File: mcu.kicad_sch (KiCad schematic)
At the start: 20 parts, among them J12 MCU_GPIOS1, J4 MCU_GPIOS2, J5 FTDI_6P, J6 AVR-ISP-6, U2 ATmega168A-A, Y1 16M

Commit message: printed pdf from schematics
Signed-off-by: Mika Laitio <lamikr@gmail.com>
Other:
- company: (none) -> Mika Laitio
- title: (none) -> I2S Audio to AES/EBU Optical Toslink
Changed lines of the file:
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@@
   (paper "A4")
   (title_block
+    (title "I2S Audio to AES/EBU Optical Toslink")
     (date "2023-12-26")
     (rev "v0.1")
+    (company "Mika Laitio")
   )
   (junction (at 59.055 38.1) (diameter 0) (color 0 0 0 0)

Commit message: added mpn and sku_digikey numbers for bom
Signed-off-by: Mika Laitio <lamikr@gmail.com>
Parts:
- C10, C11: MFR (none) -> Murata; MPN (none) -> GJM1555C1H160GB01D; SKU_DIGIKEY (none) -> 490-8081-1-ND
- C12, C6, C7, C8, C9: MFR (none) -> Murata; MPN (none) -> GRM033R61A104ME15D; SKU_DIGIKEY (none) -> 490-5405-1-ND
- J4: MFR (none) -> Würth Elektronik; MPN (none) -> 61300311121; Price (none) -> 0.13; SKU_DIGIKEY (none) -> 732-5316-ND
- J5: Notes (none) -> 1x20; Price (none) -> 0.43; SKU_DIGIKEY (none) -> 10129378-920001BLF-ND
- J6: MFR (none) -> Amphenol ICC (FCI); MPN (none) -> 75869-131LF; Notes (none) -> 2x3 with plastic; Price (none) -> 0.88; SKU_DIGIKEY (none) -> 609-2845-ND
- R1, R3: MFR (none) -> Yageo; MPN (none) -> RC0402FR-074K7L; Price (none) -> 0.1; SKU_DIGIKEY (none) -> 311-4.7KLRCT-ND
- R2: MFR (none) -> Yageo; MPN (none) -> RC0402FR-071K5L; Price (none) -> 0.1; SKU_DIGIKEY (none) -> 311-1.50KLRCT-ND
- R4: MFR (none) -> Yageo; MPN (none) -> RC0402FR-070RL; Price (none) -> 0.1; SKU_DIGIKEY (none) -> 311-0.0LRCT-ND
- R5: MFR (none) -> Yageo; MPN (none) -> RC0402FR-0710KL; Price (none) -> 0.1; SKU_DIGIKEY (none) -> 311-10.0KLRCT-ND
- U2: MFR (none) -> Microshell; MPN (none) -> ATMEGA168A-AUR; Price (none) -> 2.36; SKU_DIGIKEY (none) -> ATMEGA168A-AURTR-ND
- Y1: MFR (none) -> Abracon LLC; MPN (none) -> ABM7-16.000MHZ-D2Y-T; Price (none) -> 0.67; SKU_DIGIKEY (none) -> 535-9840-1-ND; SKU_digikey 535-9840-1-ND -> (none)

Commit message: added led that was missing from bom
Signed-off-by: Mika Laitio <lamikr@gmail.com>
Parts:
- D1: MFR (none) -> QT Brightek; MPN (none) -> QBLP631-AG; Price (none) -> 0.30; SKU_DIGIKEY (none) -> 1516-1082-1-ND
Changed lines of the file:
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@@
       (effects (font (size 1.27 1.27)) hide)
     )
-    (property "Price" "" (at 261.62 63.5 0)
+    (property "Price" "0.30" (at 261.62 63.5 0)
       (effects (font (size 1.27 1.27)) hide)
     )
+    (property "MFR" "QT Brightek" (at 261.62 63.5 0)
+      (effects (font (size 1.27 1.27)) hide)
+    )
+    (property "MPN" "QBLP631-AG" (at 261.62 63.5 0)
+      (effects (font (size 1.27 1.27)) hide)
+    )
+    (property "SKU_DIGIKEY" "1516-1082-1-ND" (at 261.62 63.5 0)
+      (effects (font (size 1.27 1.27)) hide)
+    )

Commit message: change gerber file location
Signed-off-by: Mika Laitio <lamikr@gmail.com>
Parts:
- J5: MFR (none) -> Amphenol ICC; MPN (none) -> 10129378-920001BLF-ND
- J6: MFR Amphenol ICC (FCI) -> Amphenol ICC
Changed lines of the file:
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@@
       (effects (font (size 1.27 1.27)) hide)
     )
-    (property "MFR" "Amphenol ICC (FCI)" (at 135.89 72.39 0)
+    (property "MFR" "Amphenol ICC" (at 135.89 72.39 0)
       (effects (font (size 1.27 1.27)) hide)
     )
@@
       (effects (font (size 1.27 1.27)) hide)
     )
+    (property "MFR" "Amphenol ICC" (at 190.5 91.44 0)
+      (effects (font (size 1.27 1.27)) hide)
+    )
+    (property "MPN" "10129378-920001BLF-ND" (at 190.5 91.44 0)
+      (effects (font (size 1.27 1.27)) hide)
+    )

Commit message: optimized bom from digikey
Signed-off-by: Mika Laitio <lamikr@gmail.com>
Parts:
- C10, C11, C12, C6, C7, C8, C9, R1, R2, R3, R4, R5: QtyOrdered (none) -> 100
- D1, J5, Y1: QtyOrdered (none) -> 10
- J4: MFR Würth Elektronik -> (none); MPN 61300311121 -> (none); Price 0.13 -> (none); SKU_DIGIKEY 732-5316-ND -> (none)
- J6: QtyOrdered (none) -> 5
- U2: QtyOrdered (none) -> 3; SKU_DIGIKEY ATMEGA168A-AURTR-ND -> ATMEGA168A-AURCT-ND
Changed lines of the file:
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@@
+      (effects (font (size 1.27 1.27)) hide)
+    )
+    (property "QtyOrdered" "" (at 84.455 121.92 0)
       (effects (font (size 1.27 1.27)) hide)
     )
@@
       (effects (font (size 1.27 1.27) italic) hide)
     )
-    (property "Datasheet" "http://ww1.microchip.com/downloads/en/DeviceDoc/ATmega48A_88A_168A-Data-Sheet-40002007A.pdf" (at 59.055 78.74 0)
+    (property "Datasheet" "~" (at 59.055 78.74 0)
       (effects (font (size 1.27 1.27)) hide)
     )
@@
       (effects (font (size 1.27 1.27)) hide)
     )
-    (property "SKU_DIGIKEY" "ATMEGA168A-AURTR-ND" (at 59.055 78.74 0)
+    (property "SKU_DIGIKEY" "ATMEGA168A-AURCT-ND" (at 59.055 78.74 0)
+      (effects (font (size 1.27 1.27)) hide)
+    )
+    (property "QtyOrdered" "3" (at 59.055 78.74 0)
       (effects (font (size 1.27 1.27)) hide)
     )
@@
       (effects (font (size 1.27 1.27)) hide)
     )
+    (property "QtyOrdered" "100" (at 198.12 81.915 0)
+      (effects (font (size 1.27 1.27)) hide)
+    )
     (pin "1")
     (pin "2")
@@
     )
     (property "SKU_DIGIKEY" "311-4.7KLRCT-ND" (at 144.145 106.68 0)
+      (effects (font (size 1.27 1.27)) hide)
+    )
+    (property "QtyOrdered" "100" (at 144.145 106.68 0)
       (effects (font (size 1.27 1.27)) hide)
     )
@@
       (effects (font (size 1.27 1.27)) hide)
     )
+    (property "QtyOrdered" "100" (at 207.645 29.845 0)
+      (effects (font (size 1.27 1.27)) hide)
+    )
     (pin "1")
     (pin "2")
@@
     )
     (property "SKU_DIGIKEY" "609-2845-ND" (at 135.89 72.39 0)
+      (effects (font (size 1.27 1.27)) hide)
+    )
+    (property "QtyOrdered" "5" (at 135.89 72.39 0)
       (effects (font (size 1.27 1.27)) hide)
     )
@@
       (effects (font (size 1.27 1.27)) hide)
     )
+    (property "QtyOrdered" "100" (at 133.985 106.68 0)
+      (effects (font (size 1.27 1.27)) hide)
+    )
     (pin "2")
     (pin "1")
@@
       (effects (font (size 1.27 1.27)) hide)
     )
+    (property "QtyOrdered" "100" (at 195.58 75.565 0)
+      (effects (font (size 1.27 1.27)) hide)
+    )
     (pin "2")
     (pin "1")
@@
     )
     (property "Price" "" (at 40.005 70.485 0)
+      (effects (font (size 1.27 1.27)) hide)
+    )
+    (property "QtyOrdered" "" (at 40.005 70.485 0)
       (effects (font (size 1.27 1.27)) hide)
     )
@@
       (effects (font (size 1.27 1.27)) hide)
     )
+    (property "QtyOrdered" "10" (at 134.62 34.925 0)
+      (effects (font (size 1.27 1.27)) hide)
+    )
     (pin "1")
     (pin "2")
@@
     )
     (property "MPN" "10129378-920001BLF-ND" (at 190.5 91.44 0)
+      (effects (font (size 1.27 1.27)) hide)
+    )
+    (property "QtyOrdered" "10" (at 190.5 91.44 0)
       (effects (font (size 1.27 1.27)) hide)
     )
@@
       (effects (font (size 1.27 1.27)) hide)
     )
+    (property "QtyOrdered" "100" (at 194.945 29.845 0)
+      (effects (font (size 1.27 1.27)) hide)
+    )
     (pin "1")
     (pin "2")
@@
       (effects (font (size 1.27 1.27)) hide)
     )
+    (property "QtyOrdered" "100" (at 34.925 52.07 0)
+      (effects (font (size 1.27 1.27)) hide)
+    )
     (pin "1")
     (pin "2")
@@
       (effects (font (size 1.27 1.27)) hide)
     )
+    (property "QtyOrdered" "100" (at 144.145 41.275 0)
+      (effects (font (size 1.27 1.27)) hide)
+    )
     (pin "2")
     (pin "1")
@@
       (effects (font (size 1.27 1.27)) hide)
     )
+    (property "QtyOrdered" "10" (at 261.62 63.5 0)
+      (effects (font (size 1.27 1.27)) hide)
+    )
     (pin "1")
     (pin "2")
@@
       (effects (font (size 1.27 1.27)) hide)
     )
+    (property "QtyOrdered" "100" (at 220.345 29.845 0)
+      (effects (font (size 1.27 1.27)) hide)
+    )
     (pin "1")
     (pin "2")
@@
       (effects (font (size 1.27 1.27)) hide)
     )
-    (property "MFR" "Würth Elektronik" (at 98.425 109.855 0)
-      (effects (font (size 1.27 1.27)) hide)
-    )
-    (property "MPN" "61300311121" (at 98.425 109.855 0)
+    (property "MFR" "" (at 98.425 109.855 0)
+      (effects (font (size 1.27 1.27)) hide)
+    )
+    (property "MPN" "" (at 98.425 109.855 0)
       (effects (font (size 1.27 1.27)) hide)
     )
@@
       (effects (font (size 1.27 1.27)) hide)
     )
-    (property "Price" "0.13" (at 98.425 109.855 0)
-      (effects (font (size 1.27 1.27)) hide)
-    )
-    (property "SKU_DIGIKEY" "732-5316-ND" (at 98.425 109.855 0)
+    (property "Price" "" (at 98.425 109.855 0)
+      (effects (font (size 1.27 1.27)) hide)
+    )
+    (property "SKU_DIGIKEY" "" (at 98.425 109.855 0)
+      (effects (font (size 1.27 1.27)) hide)
+    )
+    (property "QtyOrdered" "" (at 98.425 109.855 0)
       (effects (font (size 1.27 1.27)) hide)
     )
@@
       (effects (font (size 1.27 1.27)) hide)
     )
+    (property "QtyOrdered" "100" (at 193.04 68.58 0)
+      (effects (font (size 1.27 1.27)) hide)
+    )
     (pin "1")
     (pin "2")
@@
       (effects (font (size 1.27 1.27)) hide)
     )
+    (property "QtyOrdered" "100" (at 144.145 28.575 0)
+      (effects (font (size 1.27 1.27)) hide)
+    )
     (pin "2")
     (pin "1")
@@
       (effects (font (size 1.27 1.27)) hide)
     )
+    (property "QtyOrdered" "100" (at 251.46 63.5 0)
+      (effects (font (size 1.27 1.27)) hide)
+    )

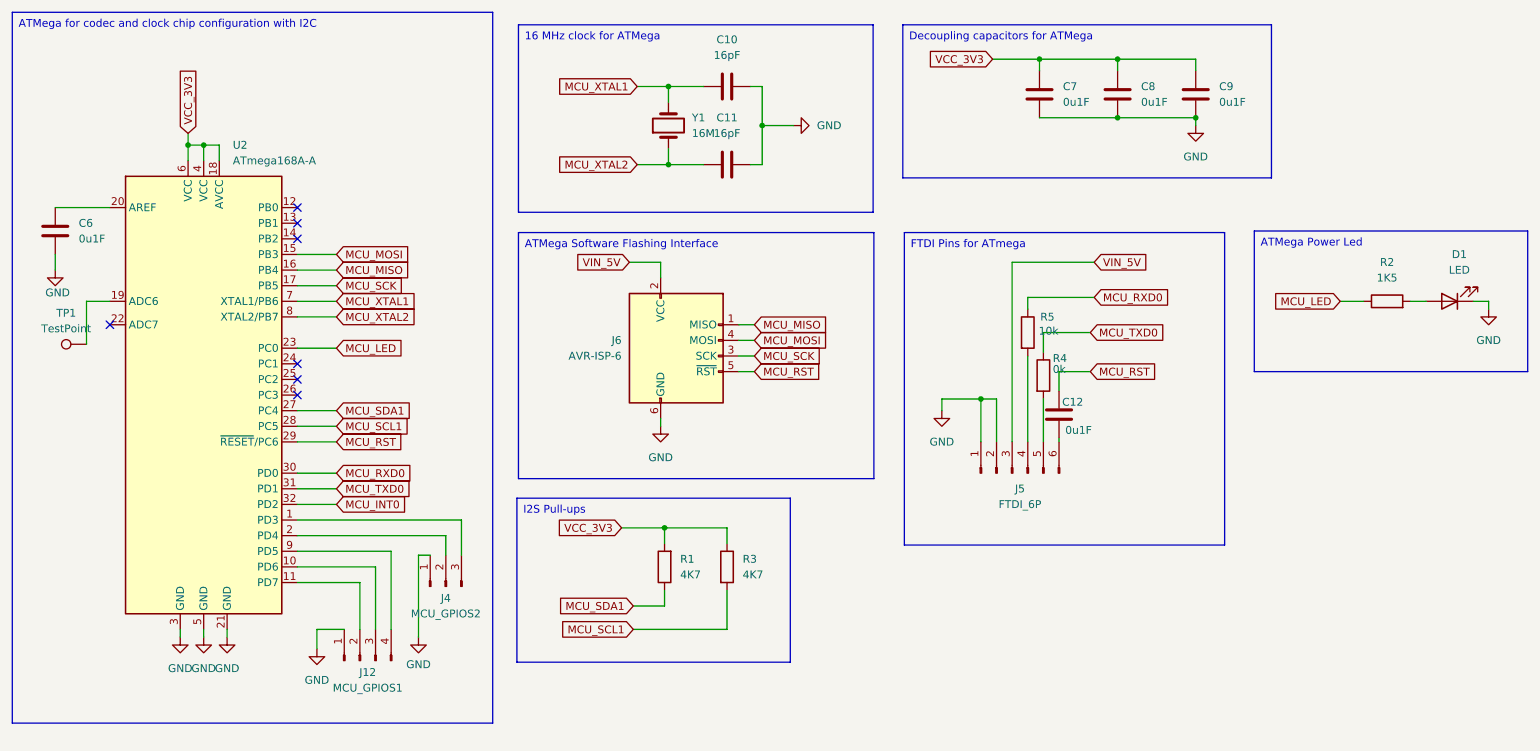
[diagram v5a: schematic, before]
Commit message: various updates
- removed duplicates 5V power connectors
- now the whole pcb is always powered via 6 pin
  atmega avr isp connector
- added connector for wm8805 rx0 and rx1
- added labels for jumpers/connectors
- moved the orientation of existing connecors
- moved the location of ldo close to
  6 pin avr isp connector

Signed-off-by: Mika Laitio <lamikr@gmail.com>
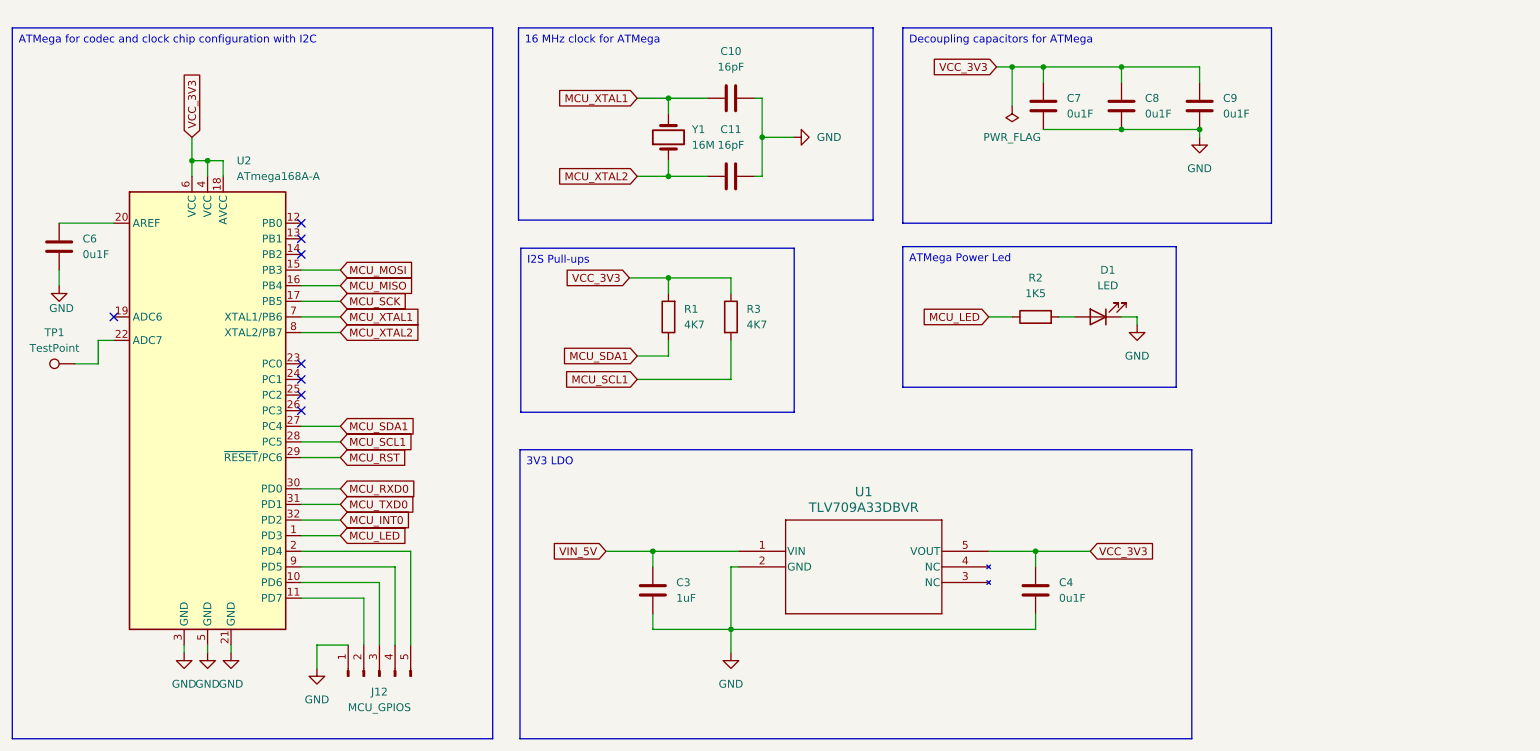
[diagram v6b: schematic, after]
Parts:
- removed C12: 0u1F, Capacitor_SMD:C_0402_1005Metric, symbol Device:C
- removed J4: MCU_GPIOS2, Connector_PinHeader_2.54mm:PinHeader_1x03_P2.54mm_Vertical, symbol Connector:Conn_01x03_Pin
- removed J5: FTDI_6P, Connector_PinHeader_2.54mm:PinHeader_1x06_P2.54mm_Vertical, symbol Connector:Conn_01x06_Pin
- removed J6: AVR-ISP-6, Connector_PinHeader_2.54mm:PinHeader_2x03_P2.54mm_Vertical, symbol Connector:AVR-ISP-6
- removed R4: 0k, Resistor_SMD:R_0402_1005Metric, symbol Device:R
- removed R5: 10k, Resistor_SMD:R_0402_1005Metric, symbol Device:R
- added C3: 1uF, Capacitor_SMD:C_0402_1005Metric, symbol Device:C
- added C4: 0u1F, Capacitor_SMD:C_0402_1005Metric, symbol Device:C
- added U1: TLV709A33DBVR, lamikr_audio:SOT-23-5_DBV_TEX, symbol lamikr_tlv709:PTLV709A33DBVR
- J12: value MCU_GPIOS1 -> MCU_GPIOS; footprint Connector_PinHeader_2.54mm:PinHeader_1x04_P2.54mm_Vertical -> Connector_PinHeader_2.54mm:PinHeader_1x05_P2.54mm_Vertical; symbol Connector:Conn_01x04_Pin -> Connector:Conn_01x05_Pin
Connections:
- net GND: now also C3.2, C4.2, U1.2 (GND)
- net MCU_LED: now also U2.1 (PD3); no longer U2.23 (PC0)
- net VCC_3V3: now also C4.1, U1.5 (VOUT)
- net VIN_5V: now also C3.1, U1.1 (VIN)
- net at U2.19 (ADC6): no longer TP1.1
- net at U2.2 (PD4): now also J12.5 (Pin_5)
- net at U2.22 (ADC7): now also TP1.1
- no-connect marks 7 -> 8
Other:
- moved on the sheet: C10, C11, C6, C7, C8, C9, D1, R1, R2, R3, TP1, U2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

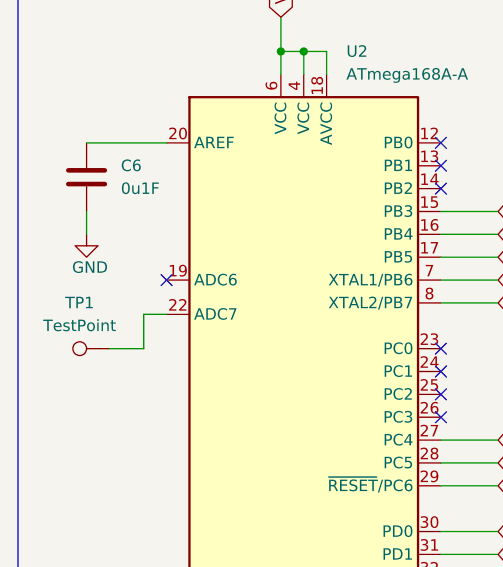
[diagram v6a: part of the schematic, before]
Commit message: finished v0.2 design
- mcu ftdi serial connector reset pin
  to 3v3 instead of 5v
- 3.3v pull-up resistor, cap and diode for mcu reset
- mcu reset button
- solder paste clearance -20% for
  mcu, codec, clk gen and ldo to help
  spreading pasta to small pins close to
  ech others

Signed-off-by: Mika Laitio <lamikr@gmail.com>
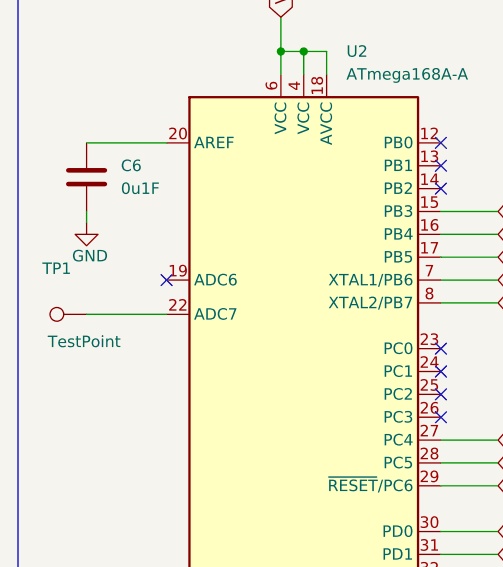
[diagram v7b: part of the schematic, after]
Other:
- moved on the sheet: TP1
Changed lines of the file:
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@@
 	(title_block
 		(title "I2S Audio to AES/EBU Optical Toslink")
-		(date "2023-12-26")
-		(rev "v0.1")
+		(date "2024-03-18")
+		(rev "v0.2")
 		(company "Mika Laitio")
 	)
@@
 	(wire
 		(pts
-			(xy 41.91 69.85) (xy 44.45 69.85)
-		)
-		(stroke
-			(width 0)
-			(type default)
-		)
-	)
-	(wire
-		(pts
 			(xy 149.86 30.48) (xy 148.59 30.48)
 		)
@@
 	(wire
 		(pts
-			(xy 35.56 58.42) (xy 35.56 60.96)
+			(xy 35.56 58.42) (xy 35.56 59.69)
 		)
 		(stroke
@@
 	(wire
 		(pts
+			(xy 35.56 69.85) (xy 44.45 69.85)
+		)
+		(stroke
+			(width 0)
+			(type default)
+		)
+	)
+	(wire
+		(pts
 			(xy 74.93 68.58) (xy 81.28 68.58)
 		)
@@
 	(wire
 		(pts
-			(xy 41.91 73.66) (xy 41.91 69.85)
-		)
-		(stroke
-			(width 0)
-			(type default)
-		)
-	)
-	(wire
-		(pts
 			(xy 132.08 116.84) (xy 144.78 116.84)
 		)
@@
 		(pts
 			(xy 82.55 119.38) (xy 77.47 119.38)
-		)
-		(stroke
-			(width 0)
-			(type default)
-		)
-	)
-	(wire
-		(pts
-			(xy 38.1 73.66) (xy 41.91 73.66)
 		)
 		(stroke
@@
 	(symbol
 		(lib_id "power:GND")
-		(at 35.56 60.96 0)
+		(at 35.56 59.69 0)
 		(unit 1)
 		(exclude_from_sim no)
@@
 		(dnp no)
 		(property "Reference" "#PWR05"
-			(at 35.56 67.31 0)
+			(at 35.56 66.04 0)
 			(effects
 				(font
@@
 		)
 		(property "Value" "GND"
-			(at 35.941 64.643 0)
+			(at 35.941 63.373 0)
 			(effects
 				(font
@@
 		)
 		(property "Footprint" ""
-			(at 35.56 60.96 0)
+			(at 35.56 59.69 0)
 			(effects
 				(font
@@
 		)
 		(property "Datasheet" ""
-			(at 35.56 60.96 0)
+			(at 35.56 59.69 0)
 			(effects
 				(font
@@
 		)
 		(property "Description" "Power symbol creates a global label with name \"GND\" , ground"
-			(at 35.56 60.96 0)
+			(at 35.56 59.69 0)
 			(effects
 				(font
@@
 	(symbol
 		(lib_id "Connector:TestPoint")
-		(at 38.1 73.66 90)
+		(at 35.56 69.85 90)
 		(unit 1)
 		(exclude_from_sim no)
@@
 		(on_board yes)
 		(dnp no)
-		(fields_autoplaced yes)
 		(property "Reference" "TP1"
-			(at 34.798 68.58 90)
+			(at 32.258 64.77 90)
 			(effects
 				(font
@@
 		)
 		(property "Value" "TestPoint"
-			(at 34.798 71.12 90)
+			(at 35.306 72.898 90)
 			(effects
 				(font
@@
 		)
 		(property "Footprint" "TestPoint:TestPoint_Pad_D1.0mm"
-			(at 38.1 68.58 0)
+			(at 35.56 64.77 0)
 			(effects
 				(font
@@
 		)
 		(property "Datasheet" "~"
-			(at 38.1 68.58 0)
+			(at 35.56 64.77 0)
 			(effects
 				(font
@@
 		)
 		(property "Description" "test point"
-			(at 38.1 73.66 0)
+			(at 35.56 69.85 0)
 			(effects
 				(font
@@
 		)
 		(property "Notes" ""
-			(at 38.1 73.66 0)
+			(at 35.56 69.85 0)
 			(effects
 				(font
@@
 		)
 		(property "Price" ""
-			(at 38.1 73.66 0)
+			(at 35.56 69.85 0)
 			(effects
 				(font
@@
 		)
 		(property "QtyOrdered" ""
-			(at 38.1 73.66 0)
-			(effects
-				(font
+			(at 35.56 69.85 0)
+			(effects
+				(font

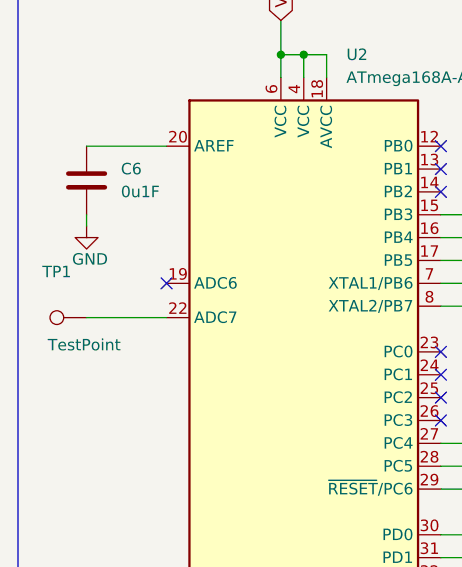
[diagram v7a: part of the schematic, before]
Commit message: component footprint updates
- 0402 caps and resistors to 0603
- reset pin-header to reset button

Signed-off-by: Mika Laitio <lamikr@gmail.com>
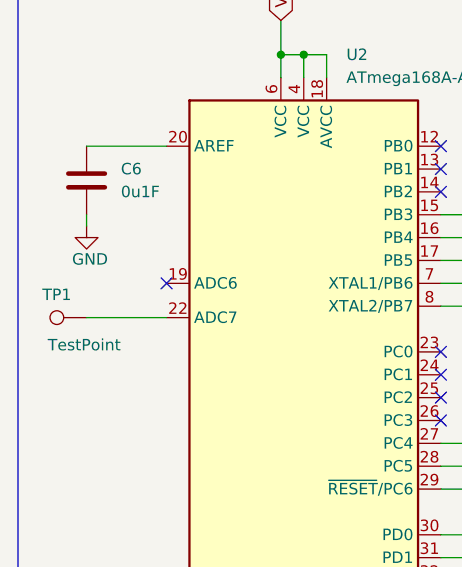
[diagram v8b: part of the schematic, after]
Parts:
- C3, C4, C6, C9: footprint Capacitor_SMD:C_0402_1005Metric -> Capacitor_SMD:C_0603_1608Metric
- R2: footprint Resistor_SMD:R_0402_1005Metric -> Resistor_SMD:R_0603_1608Metric
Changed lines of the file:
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@@
 			)
 		)
-		(property "Footprint" "Capacitor_SMD:C_0402_1005Metric"
+		(property "Footprint" "Capacitor_SMD:C_0603_1608Metric"
 			(at 133.0452 114.3 0)
 			(effects
@@
 		(dnp no)
 		(property "Reference" "TP1"
-			(at 32.258 64.77 90)
+			(at 32.258 67.31 90)
 			(effects
 				(font
@@
 			)
 		)
-		(property "Footprint" "Capacitor_SMD:C_0402_1005Metric"
+		(property "Footprint" "Capacitor_SMD:C_0603_1608Metric"
 			(at 195.2752 114.3 0)
 			(effects
@@
 			)
 		)
-		(property "Footprint" "Capacitor_SMD:C_0402_1005Metric"
+		(property "Footprint" "Capacitor_SMD:C_0603_1608Metric"
 			(at 36.5252 58.42 0)
 			(effects
@@
 			)
 		)
-		(property "Footprint" "Capacitor_SMD:C_0402_1005Metric"
+		(property "Footprint" "Capacitor_SMD:C_0603_1608Metric"
 			(at 221.9452 35.56 0)
 			(effects
@@
 			)
 		)
-		(property "Footprint" "Resistor_SMD:R_0402_1005Metric"
+		(property "Footprint" "Resistor_SMD:R_0603_1608Metric"
 			(at 194.31 67.818 90)
 			(effects
